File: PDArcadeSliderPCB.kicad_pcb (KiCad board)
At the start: 2 copper layers, 100 x 63.6 mm, 30 parts, among them J1 Conn_01x01_Male, J10 topgroundhatching, J2 Conn_01x06_Male, J6 Conn_01x01_Male, J7 Conn_01x01_Male, J8 Conn_01x01_Male, J9 Conn_01x01_Male, U1 testsensorg, U2 testsensorg, U3 testsensorg, U4 testsensorg, U5 testsensorg, U6 testsensorg

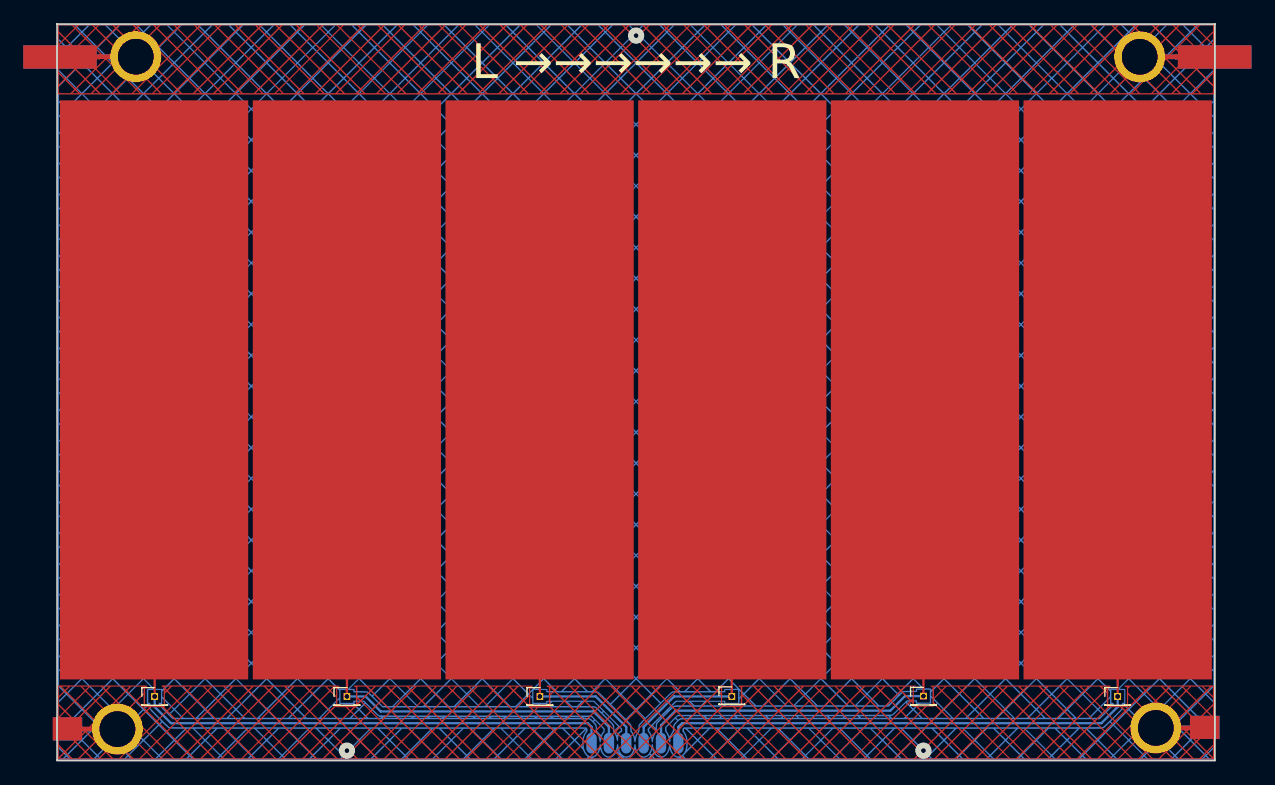
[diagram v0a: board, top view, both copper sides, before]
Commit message: Changed through holes on CapSense traces. Sent to production
Changed through holes on CapSense traces. Sent to production
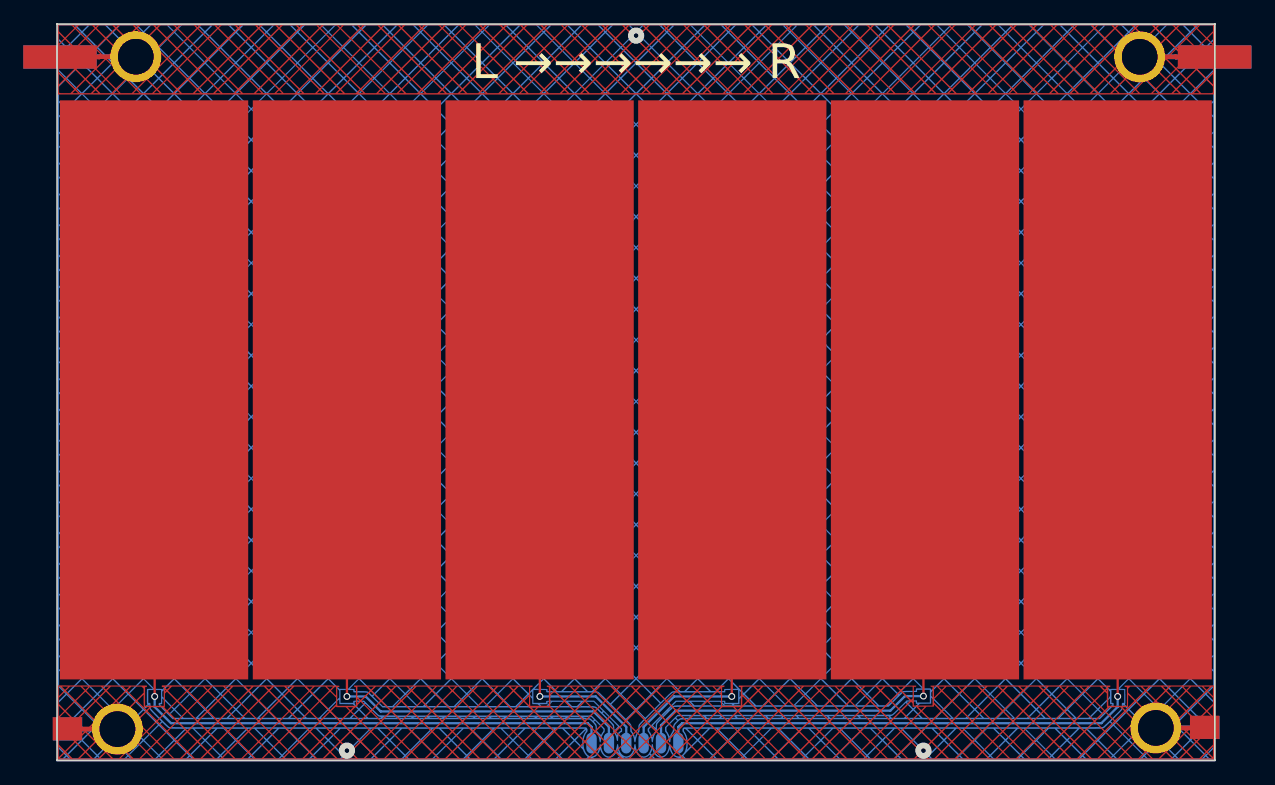
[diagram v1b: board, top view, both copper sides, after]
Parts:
- removed J1, J6 (x2), J7, J8, J9: Conn_01x01_Male, Connector_PinHeader_1.27mm:PinHeader_1x01_P1.27mm_Vertical
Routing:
- net Net-(J2-Pad6): vias 0 -> 1
- net Net-(J2-Pad5): vias 0 -> 1
- net Net-(J2-Pad4): vias 0 -> 1
- net Net-(J2-Pad3): vias 0 -> 1
- net Net-(J2-Pad2): vias 0 -> 1
- net Net-(J1-Pad1): vias 0 -> 1

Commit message: Version with ground hatching failed. Changes and fixes
without ground hatching
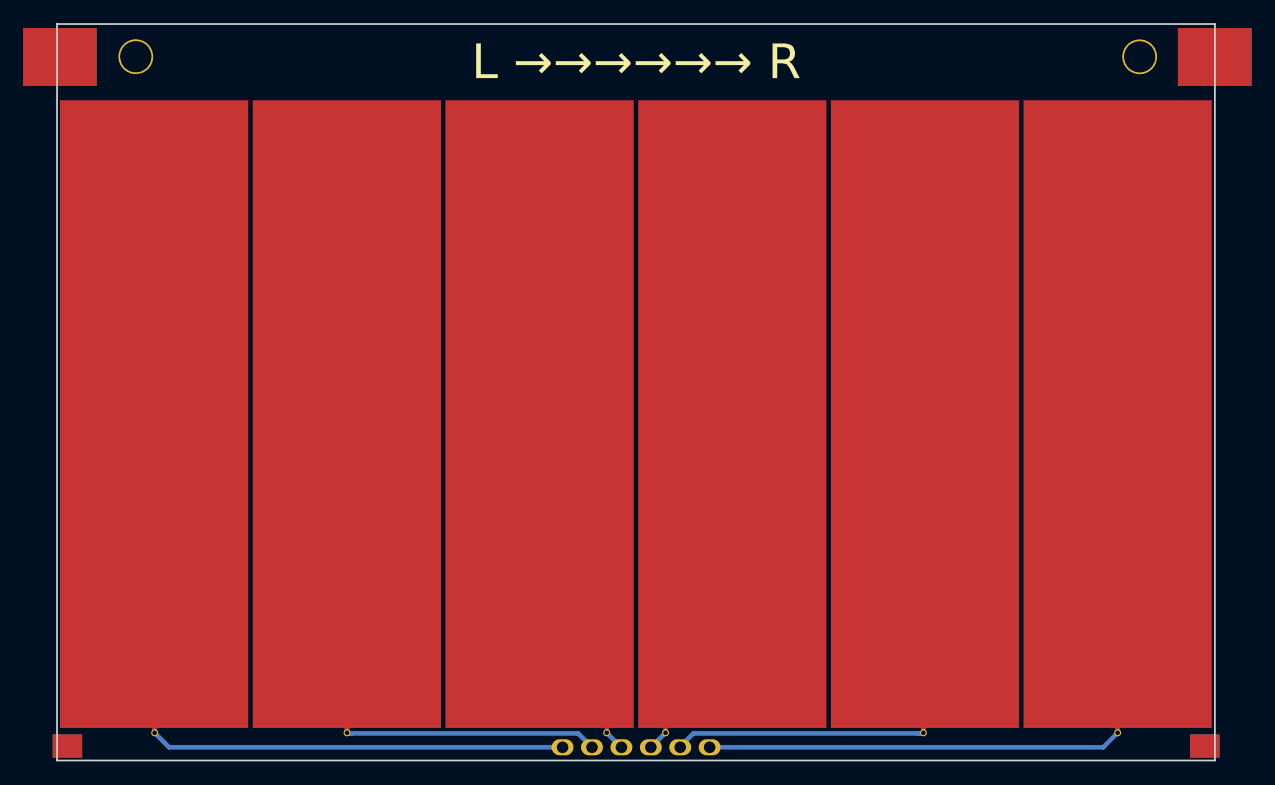
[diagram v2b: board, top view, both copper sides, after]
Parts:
- removed the G*** at (150.1, 135.4)
- removed J10: topgroundhatching, PDArcadeSliderPCB:TopHatching
- removed the REF** at (105.3, 166.2)
- removed the REF** at (195.0, 166.2)
- added REF**: MountingHole_2.2mm_M2_Pad, MountingHole:MountingHole_2.2mm_M2_Pad, F.Cu at (142.0, 164.6)
- added REF**: MountingHole_2.2mm_M2_Pad, MountingHole:MountingHole_2.2mm_M2_Pad, F.Cu at (191.7, 163.3)
- added REF**: MountingHole_2.2mm_M2_Pad, MountingHole:MountingHole_2.2mm_M2_Pad, F.Cu at (174.9, 163.3)
- added REF**: MountingHole_2.2mm_M2_Pad, MountingHole:MountingHole_2.2mm_M2_Pad, F.Cu at (158.4, 164.6)
- added REF**: MountingHole_2.2mm_M2_Pad, MountingHole:MountingHole_2.2mm_M2_Pad, F.Cu at (125.1, 163.4)
- added REF**: MountingHole_2.2mm_M2_Pad, MountingHole:MountingHole_2.2mm_M2_Pad, F.Cu at (108.5, 163.4)
- moved J2 0.36 mm to (155.8, 166.1)
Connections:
- REF** pad 1: GND -> (no net) (x10)
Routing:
- net GND: track 42.0 -> 0.15 mm, vias 3 -> 0
- net Net-(J2-Pad3): track 36.6 -> 76.8 mm, vias 1 -> 0
- net Net-(J2-Pad4): track 37.0 -> 75.4 mm, vias 1 -> 0
- net Net-(J1-Pad1): track 106.3 -> 102.4 mm, vias 1 -> 0
- net Net-(J2-Pad6): track 67.2 -> 63.8 mm, vias 1 -> 0
- net Net-(J2-Pad5): track 51.6 -> 49.9 mm, vias 1 -> 0
- net Net-(J2-Pad2): track 70.1 -> 69.0 mm, vias 1 -> 0

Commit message: little bigger pads, deleted trash
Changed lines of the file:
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@@
     (thickness 1.6)
     (drawings 7)
-    (tracks 77)
+    (tracks 75)
     (modules 26)
     (nets 8)
@@
       (dimension_precision 1)
     )
-    (pad_size 1.4 1.9)
-    (pad_drill 1)
+    (pad_size 0.6 0.6)
+    (pad_drill 0.4)
     (pad_to_mask_clearance 0.1)
     (solder_mask_min_width 0.15)
@@
     (fp_circle (center 0 0) (end 2.2 0) (layer "Cmts.User") (width 0.15))
     (fp_circle (center 0 0) (end 2.45 0) (layer "F.CrtYd") (width 0.05))
-    (pad "1" thru_hole circle (at 0.22 -5.58 270) (size 0.6 0.6) (drill 0.4) (layers *.Cu *.Mask)
+    (pad "1" thru_hole circle (at 0.27 -5.58 270) (size 0.6 0.6) (drill 0.4) (layers *.Cu *.Mask)
       (net 5 "Net-(J2-Pad4)"))
   )
@@
       (effects (font (size 1 1) (thickness 0.15)))
     )
-    (pad "1" thru_hole circle (at 1.54 0 270) (size 0.6 0.6) (drill 0.4) (layers *.Cu *.Mask)
+    (pad "1" thru_hole circle (at 1.59 0 270) (size 0.6 0.6) (drill 0.4) (layers *.Cu *.Mask)
       (net 1 "Net-(J1-Pad1)"))
   )
@@
     (fp_circle (center 0 0) (end 2.2 0) (layer "Cmts.User") (width 0.15))
     (fp_circle (center 0 0) (end 2.45 0) (layer "F.CrtYd") (width 0.05))
-    (pad "1" thru_hole circle (at 1.52 0 270) (size 0.6 0.6) (drill 0.4) (layers *.Cu *.Mask)
+    (pad "1" thru_hole circle (at 1.57 0 270) (size 0.6 0.6) (drill 0.4) (layers *.Cu *.Mask)
       (net 7 "Net-(J2-Pad2)"))
   )
@@
       (effects (font (size 1 1) (thickness 0.15)))
     )
-    (pad "1" thru_hole circle (at 0.23 5.74 270) (size 0.6 0.6) (drill 0.4) (layers *.Cu *.Mask)
+    (pad "1" thru_hole circle (at 0.28 5.74 270) (size 0.6 0.6) (drill 0.4) (layers *.Cu *.Mask)
       (net 6 "Net-(J2-Pad3)"))
   )
@@
       (effects (font (size 1 1) (thickness 0.15)))
     )
-    (pad "1" thru_hole circle (at 1.49 0 270) (size 0.6 0.6) (drill 0.4) (layers *.Cu *.Mask)
+    (pad "1" thru_hole circle (at 1.54 0 270) (size 0.6 0.6) (drill 0.4) (layers *.Cu *.Mask)
       (net 4 "Net-(J2-Pad5)"))
   )
@@
     (fp_circle (center 0 0) (end 2.2 0) (layer "Cmts.User") (width 0.15))
     (fp_circle (center 0 0) (end 2.45 0) (layer "F.CrtYd") (width 0.05))
-    (pad "1" thru_hole circle (at 1.49 0 270) (size 0.6 0.6) (drill 0.4) (layers *.Cu *.Mask)
+    (pad "1" thru_hole circle (at 1.54 0 270) (size 0.6 0.6) (drill 0.4) (layers *.Cu *.Mask)
       (net 3 "Net-(J2-Pad6)"))
   )
@@
       (effects (font (size 1 1) (thickness 0.15)))
     )
-    (pad "1" connect rect (at -13.15 10.158 270) (size 54.2 16.256) (layers "F.Cu")
+    (pad "1" connect rect (at -13.125 10.158 270) (size 54.25 16.256) (layers "F.Cu")
       (net 1 "Net-(J1-Pad1)"))
   )
@@
       (effects (font (size 1 1) (thickness 0.15)))
     )
-    (pad "1" connect rect (at -13.15 10.16 270) (size 54.2 16.256) (layers "F.Cu")
+    (pad "1" connect rect (at -13.125 10.16 270) (size 54.25 16.256) (layers "F.Cu")
       (net 6 "Net-(J2-Pad3)"))
   )
@@
       (effects (font (size 1 1) (thickness 0.15)))
     )
-    (pad "1" connect rect (at -13.15 10.16 270) (size 54.2 16.256) (layers "F.Cu")
+    (pad "1" connect rect (at -13.125 10.16 270) (size 54.25 16.256) (layers "F.Cu")
       (net 4 "Net-(J2-Pad5)"))
   )
@@
       (effects (font (size 1 1) (thickness 0.15)))
     )
-    (pad "1" connect rect (at -13.15 10.16 270) (size 54.2 16.256) (layers "F.Cu")
+    (pad "1" connect rect (at -13.125 10.16 270) (size 54.25 16.256) (layers "F.Cu")
       (net 7 "Net-(J2-Pad2)"))
   )
@@
       (effects (font (size 1 1) (thickness 0.15)))
     )
-    (pad "1" connect rect (at -13.15 10.16 270) (size 54.2 16.256) (layers "F.Cu")
+    (pad "1" connect rect (at -13.125 10.16 270) (size 54.25 16.256) (layers "F.Cu")
       (net 5 "Net-(J2-Pad4)"))
   )
@@
       (effects (font (size 1 1) (thickness 0.15)))
     )
-    (pad "1" connect rect (at -13.15 10.173 270) (size 54.2 16.256) (layers "F.Cu")
+    (pad "1" connect rect (at -13.125 10.173 270) (size 54.25 16.256) (layers "F.Cu")
       (net 3 "Net-(J2-Pad6)"))
   )
@@
   (gr_line (start 200.075 103.65) (end 200.075 167.24) (layer "Edge.Cuts") (width 0.15))
   (gr_line (start 200.075 167.24) (end 100.1 167.24) (layer "Edge.Cuts") (width 0.15))
+  (segment (start 148.83 166.1) (end 148.76 166.1) (width 0.4) (layer "B.Cu") (net 5))
+  (segment (start 148.76 166.1) (end 147.56 164.9) (width 0.4) (layer "B.Cu") (net 5))
+  (segment (start 151.44 166.1) (end 152.64 164.9) (width 0.4) (layer "B.Cu") (net 6))
   (segment (start 152.64 164.85) (end 152.64 143.094) (width 0.4) (layer "F.Cu") (net 6))
   (segment (start 152.64 143.094) (end 158.404 137.33) (width 0.4) (layer "F.Cu") (net 6))
-  (segment (start 151.37 166.1) (end 151.39 166.1) (width 0.4) (layer "B.Cu") (net 6))
-  (segment (start 151.39 166.1) (end 152.64 164.85) (width 0.4) (layer "B.Cu") (net 6))
   (segment (start 147.56 164.85) (end 147.56 143.123) (width 0.4) (layer "F.Cu") (net 5))
   (segment (start 147.56 143.123) (end 141.767 137.33) (width 0.4) (layer "F.Cu") (net 5))
   (segment (start 148.83 166.1) (end 148.81 166.1) (width 0.4) (layer "B.Cu") (net 5))
-  (segment (start 148.81 166.1) (end 147.56 164.85) (width 0.4) (layer "B.Cu") (net 5))
   (segment (start 191.68 164.7) (end 191.68 164.46) (width 0.4) (layer "F.Cu") (net 1))
   (segment (start 191.68 164.46) (end 191.68 137.25) (width 0.4) (layer "F.Cu") (net 1))
@@
   (segment (start 125.519999 164.899999) (end 145.089999 164.899999) (width 0.4) (layer "B.Cu") (net 4))
   (segment (start 125.189999 164.899999) (end 125.14 164.85) (width 0.4) (layer "B.Cu") (net 4))
-  (segment (start 151.37 166.1) (end 151.38 166.1) (width 0.4) (layer "B.Cu") (net 6))
   (segment (start 156.45 166.1) (end 190.43 166.1) (width 0.4) (layer "B.Cu") (net 1))
   (segment (start 190.43 166.1) (end 191.68 164.85) (width 0.4) (layer "B.Cu") (net 1))
@@
   (segment (start 153.91 166.1) (end 153.91 166.04) (width 0.4) (layer "B.Cu") (net 7))
   (segment (start 153.91 166.04) (end 155.050001 164.899999) (width 0.4) (layer "B.Cu") (net 7))
-  (segment (start 151.32 166.1) (end 151.32 166.01) (width 0.4) (layer "B.Cu") (net 6))
   (segment (start 174.909 135.372) (end 175.041 135.24) (width 0.4) (layer "F.Cu") (net 7))
   (segment (start 175.036 135.245) (end 175.041 135.24) (width 0.4) (layer "F.Cu") (net 7))

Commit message: Changes, sent to production
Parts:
- removed the REF** at (142.0, 164.6)
- removed the REF** at (191.7, 163.3)
- removed the REF** at (174.9, 163.3)
- removed the REF** at (158.4, 164.6)
- removed the REF** at (125.1, 163.4)
- removed the REF** at (108.5, 163.4)
- moved REF** 0.20 mm to (196.7, 167.2)
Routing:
- net Net-(J2-Pad5): track 49.9 -> 49.3 mm, vias 0 -> 1
- net Net-(J2-Pad2): track 69.0 -> 68.4 mm, vias 0 -> 1
- net Net-(J1-Pad1): track 102.4 -> 102.2 mm, vias 0 -> 1
- net Net-(J2-Pad6): track 63.8 -> 63.7 mm, vias 0 -> 1
- net Net-(J2-Pad4): track 75.4 -> 75.5 mm, vias 0 -> 1
- net Net-(J2-Pad3): track 76.6 -> 76.7 mm, vias 0 -> 1
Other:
- board size 100 x 63.6 mm -> 100 x 63.2 mm
- board text added: "Hatsune Miku Project DIVA Arcade Future Tone Slider Base PCB v1.8 by Jan de Valua based on board by azhao12345"
- board text removed: "Hatsune Miku Project DIVA Arcade Future Tone Slider Base PCB v1.5 by Jan de Valua based on board by azhao12345"
